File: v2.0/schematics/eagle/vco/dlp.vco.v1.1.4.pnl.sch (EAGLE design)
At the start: 23 parts, among them J1 PWM IN1, J4 EXP.IN1, J6 OSC OUT1

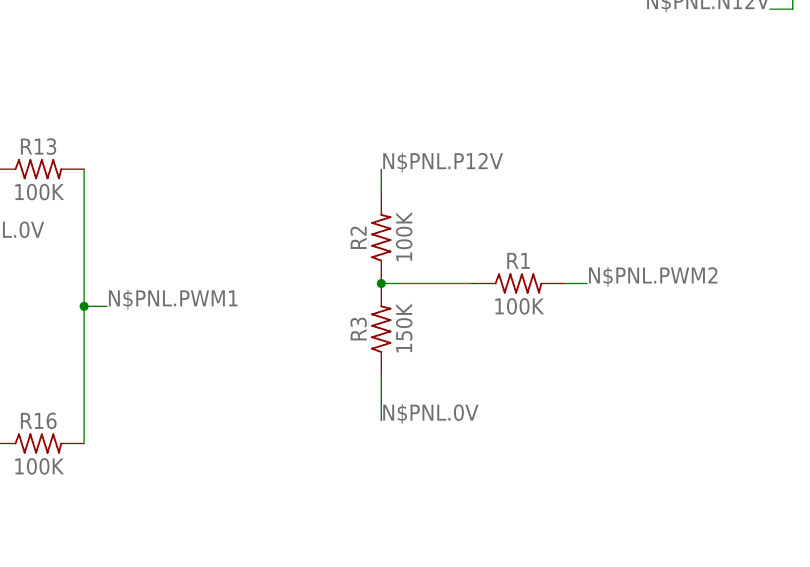
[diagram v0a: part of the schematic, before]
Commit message: Updated values for fixed PWM2
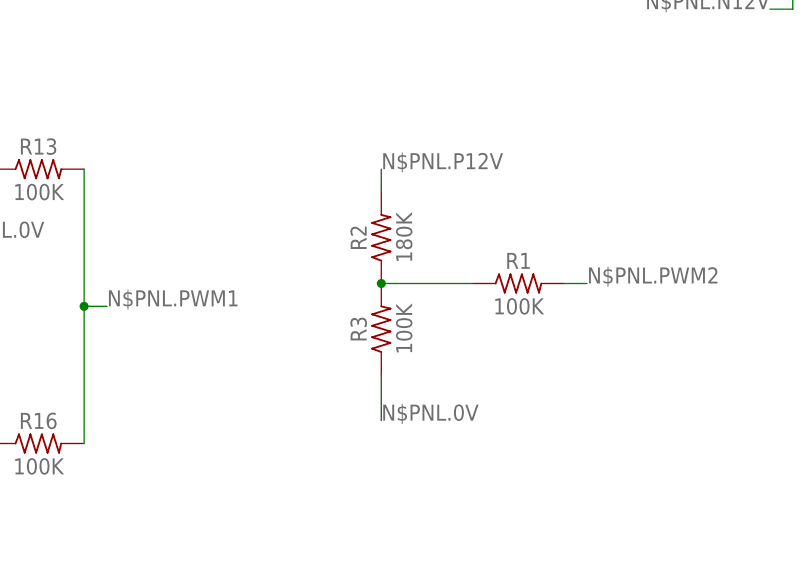
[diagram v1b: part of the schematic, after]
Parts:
- R2: value 100K -> 180K
- R3: value 150K -> 100K
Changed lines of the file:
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@@
 <part name="JP2" library="pinhead" deviceset="PINHD-1X10" device="" value="OSC2"/>
 <part name="R1" library="_common" deviceset="R" device="0309/10" value="100K"/>
-<part name="R2" library="_common" deviceset="R" device="0309/10" value="100K"/>
-<part name="R3" library="_common" deviceset="R" device="0309/10" value="150K"/>
+<part name="R2" library="_common" deviceset="R" device="0309/10" value="180K"/>
+<part name="R3" library="_common" deviceset="R" device="0309/10" value="100K"/>
 <part name="SW-LEVEL2" library="_common" deviceset="R-VAR" device="" value="50K (log)"/>
 <part name="SQ-LEVEL2" library="_common" deviceset="R-VAR" device="" value="50K (log)"/>

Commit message: Split EXP1 and 2 and added EXP2 IN Removed PWM1 ATT and added PWM2
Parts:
- removed R16, R3: 100K, _common:R0309/10
- removed R2: 180K, _common:R0309/10
- added J2: EXP.IN2, _common:JACK-M
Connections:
- removed net N$1: R1.1, R2.1, R3.2
- new net N$6: J2.HOT, R4/2.A
- net N$19: now also R1.1; no longer R16.1
- net N$4: no longer R4/2.A
- net N$PNL.0V: now also J2.GND; no longer R3.1
- net N$PNL.P12V: no longer R2.2
- net N$PNL.PWM1: no longer R16.2
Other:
- moved on the sheet: PWM1, R1
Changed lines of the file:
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@@
 <part name="PWM.ATT1" library="_common" deviceset="R-VAR" device="" value="250K (lin)"/>
 <part name="R13" library="_common" deviceset="R" device="0309/10" value="100K"/>
-<part name="R16" library="_common" deviceset="R" device="0309/10" value="100K"/>
 <part name="JP1" library="pinhead" deviceset="PINHD-1X10" device="" value="OSC1"/>
 <part name="JP2" library="pinhead" deviceset="PINHD-1X10" device="" value="OSC2"/>
 <part name="R1" library="_common" deviceset="R" device="0309/10" value="100K"/>
-<part name="R2" library="_common" deviceset="R" device="0309/10" value="180K"/>
-<part name="R3" library="_common" deviceset="R" device="0309/10" value="100K"/>
 <part name="SW-LEVEL2" library="_common" deviceset="R-VAR" device="" value="50K (log)"/>
 <part name="SQ-LEVEL2" library="_common" deviceset="R-VAR" device="" value="50K (log)"/>
@@
 <part name="R6" library="_common" deviceset="R" device="0309/10" value="100K"/>
 <part name="TUNE2" library="_common" deviceset="R-VAR" device="" value="250K (lin)"/>
+<part name="J2" library="_common" deviceset="JACK-M" device="" value="EXP.IN2"/>
 </parts>
 <sheets>
@@
 <instances>
 <instance part="J1" gate="G$1" x="5.08" y="17.78"/>
-<instance part="PWM1" gate="G$1" x="7.62" y="-20.32" rot="R270"/>
+<instance part="PWM1" gate="G$1" x="48.26" y="-10.16" rot="R270"/>
 <instance part="R14" gate="G$1" x="27.94" y="66.04" rot="R180"/>
 <instance part="R15" gate="G$1" x="17.78" y="35.56"/>
@@
 <instance part="PWM.ATT1" gate="G$1" x="12.7" y="10.16" rot="R270"/>
 <instance part="R13" gate="G$1" x="27.94" y="10.16"/>
-<instance part="R16" gate="G$1" x="27.94" y="-20.32"/>
 <instance part="JP1" gate="A" x="12.7" y="-53.34" rot="R180"/>
 <instance part="JP2" gate="A" x="55.88" y="-53.34" rot="R180"/>
-<instance part="R1" gate="G$1" x="81.28" y="-2.54"/>
-<instance part="R2" gate="G$1" x="66.04" y="2.54" rot="R90"/>
-<instance part="R3" gate="G$1" x="66.04" y="-7.62" rot="R90"/>
+<instance part="R1" gate="G$1" x="68.58" y="-10.16"/>
 <instance part="SW-LEVEL2" gate="G$1" x="147.32" y="10.16" rot="R180"/>
 <instance part="SQ-LEVEL2" gate="G$1" x="147.32" y="-20.32"/>
@@
 <instance part="R6" gate="G$1" x="96.52" y="35.56" rot="MR0"/>
 <instance part="TUNE2" gate="G$1" x="111.76" y="35.56" rot="MR270"/>
+<instance part="J2" gate="G$1" x="73.66" y="71.12" rot="MR0"/>
 </instances>
 <busses>
@@
 <segment>
 <pinref part="PWM1" gate="G$1" pin="P$1"/>
-<pinref part="R16" gate="G$1" pin="1"/>
-<wire x1="12.7" y1="-20.32" x2="22.86" y2="-20.32" width="0.1524" layer="91"/>
+<wire x1="53.34" y1="-10.16" x2="63.5" y2="-10.16" width="0.1524" layer="91"/>
+<pinref part="R1" gate="G$1" pin="1"/>
 </segment>
 </net>
@@
 <segment>
 <pinref part="PWM1" gate="G$1" pin="2"/>
-<wire x1="7.62" y1="-25.4" x2="7.62" y2="-27.94" width="0.1524" layer="91"/>
-<wire x1="7.62" y1="-27.94" x2="12.7" y2="-27.94" width="0.1524" layer="91"/>
-<label x="12.7" y="-27.94" size="1.778" layer="95"/>
+<wire x1="48.26" y1="-15.24" x2="48.26" y2="-17.78" width="0.1524" layer="91"/>
+<wire x1="48.26" y1="-17.78" x2="53.34" y2="-17.78" width="0.1524" layer="91"/>
+<label x="53.34" y="-17.78" size="1.778" layer="95"/>
 </segment>
 <segment>
@@
 </segment>
 <segment>
-<wire x1="66.04" y1="-12.7" x2="66.04" y2="-17.78" width="0.1524" layer="91"/>
-<label x="66.04" y="-17.78" size="1.778" layer="95"/>
-<pinref part="R3" gate="G$1" pin="1"/>
-</segment>
-<segment>
 <label x="76.2" y="53.34" size="1.778" layer="95" rot="MR0"/>
 <wire x1="76.2" y1="58.42" x2="66.04" y2="58.42" width="0.1524" layer="91"/>
@@
 <pinref part="R4" gate="/2" pin="E"/>
 <wire x1="66.04" y1="58.42" x2="66.04" y2="60.96" width="0.1524" layer="91"/>
+<pinref part="J2" gate="G$1" pin="GND"/>
+<wire x1="76.2" y1="68.58" x2="76.2" y2="58.42" width="0.1524" layer="91"/>
+<junction x="76.2" y="58.42"/>
 </segment>
 </net>
@@
 <segment>
 <pinref part="R13" gate="G$1" pin="2"/>
-<pinref part="R16" gate="G$1" pin="2"/>
-<wire x1="33.02" y1="10.16" x2="33.02" y2="-5.08" width="0.1524" layer="91"/>
-<label x="35.56" y="-5.08" size="1.778" layer="95"/>
-<wire x1="33.02" y1="-5.08" x2="33.02" y2="-20.32" width="0.1524" layer="91"/>
-<wire x1="33.02" y1="-5.08" x2="35.56" y2="-5.08" width="0.1524" layer="91"/>
-<junction x="33.02" y="-5.08"/>
+<label x="38.1" y="10.16" size="1.778" layer="95"/>
+<wire x1="33.02" y1="10.16" x2="38.1" y2="10.16" width="0.1524" layer="91"/>
 </segment>
 </net>
@@
 <segment>
 <pinref part="PWM1" gate="G$1" pin="1"/>
-<wire x1="7.62" y1="-15.24" x2="7.62" y2="-12.7" width="0.1524" layer="91"/>
-<wire x1="7.62" y1="-12.7" x2="10.16" y2="-12.7" width="0.1524" layer="91"/>
-<label x="10.16" y="-12.7" size="1.778" layer="95"/>
+<wire x1="48.26" y1="-5.08" x2="48.26" y2="-2.54" width="0.1524" layer="91"/>
+<wire x1="48.26" y1="-2.54" x2="50.8" y2="-2.54" width="0.1524" layer="91"/>
+<label x="50.8" y="-2.54" size="1.778" layer="95"/>
 </segment>
 <segment>
@@
 <wire x1="58.42" y1="-58.42" x2="68.58" y2="-58.42" width="0.1524" layer="91"/>
 <label x="68.58" y="-58.42" size="1.778" layer="95"/>
-</segment>
-<segment>
-<wire x1="66.04" y1="7.62" x2="66.04" y2="10.16" width="0.1524" layer="91"/>
-<label x="66.04" y="10.16" size="1.778" layer="95"/>
-<pinref part="R2" gate="G$1" pin="2"/>
 </segment>
 <segment>
@@
 <segment>
 <pinref part="R1" gate="G$1" pin="2"/>
-<label x="88.9" y="-2.54" size="1.778" layer="95"/>
-<wire x1="86.36" y1="-2.54" x2="88.9" y2="-2.54" width="0.1524" layer="91"/>
+<label x="76.2" y="-10.16" size="1.778" layer="95"/>
+<wire x1="73.66" y1="-10.16" x2="76.2" y2="-10.16" width="0.1524" layer="91"/>
 </segment>
 </net>
@@
 </segment>
 </net>
-<net name="N$1" class="0">
-<segment>
-<pinref part="R1" gate="G$1" pin="1"/>
-<wire x1="66.04" y1="-2.54" x2="76.2" y2="-2.54" width="0.1524" layer="91"/>
-<pinref part="R3" gate="G$1" pin="2"/>
-<pinref part="R2" gate="G$1" pin="1"/>
-<junction x="66.04" y="-2.54"/>
-</segment>
-</net>
 <net name="N$2" class="0">
 <segment>
@@
 <net name="N$4" class="0">
 <segment>
-<pinref part="R4" gate="/2" pin="A"/>
-<wire x1="66.04" y1="73.66" x2="66.04" y2="71.12" width="0.1524" layer="91"/>
 <pinref part="J4" gate="G$1" pin="HOT"/>
 <wire x1="48.26" y1="71.12" x2="48.26" y2="73.66" width="0.1524" layer="91"/>
 <wire x1="48.26" y1="73.66" x2="45.72" y2="73.66" width="0.1524" layer="91"/>
 <pinref part="R4" gate="/1" pin="E"/>
-<wire x1="66.04" y1="73.66" x2="48.26" y2="73.66" width="0.1524" layer="91"/>
-<junction x="48.26" y="73.66"/>
 </segment>
 </net>
@@
 </segment>
 </net>
+<net name="N$6" class="0">
+<segment>
+<pinref part="R4" gate="/2" pin="A"/>
+<wire x1="68.58" y1="73.66" x2="66.04" y2="73.66" width="0.1524" layer="91"/>
+<wire x1="66.04" y1="73.66" x2="66.04" y2="71.12" width="0.1524" layer="91"/>
+<pinref part="J2" gate="G$1" pin="HOT"/>
+</segment>
+</net>

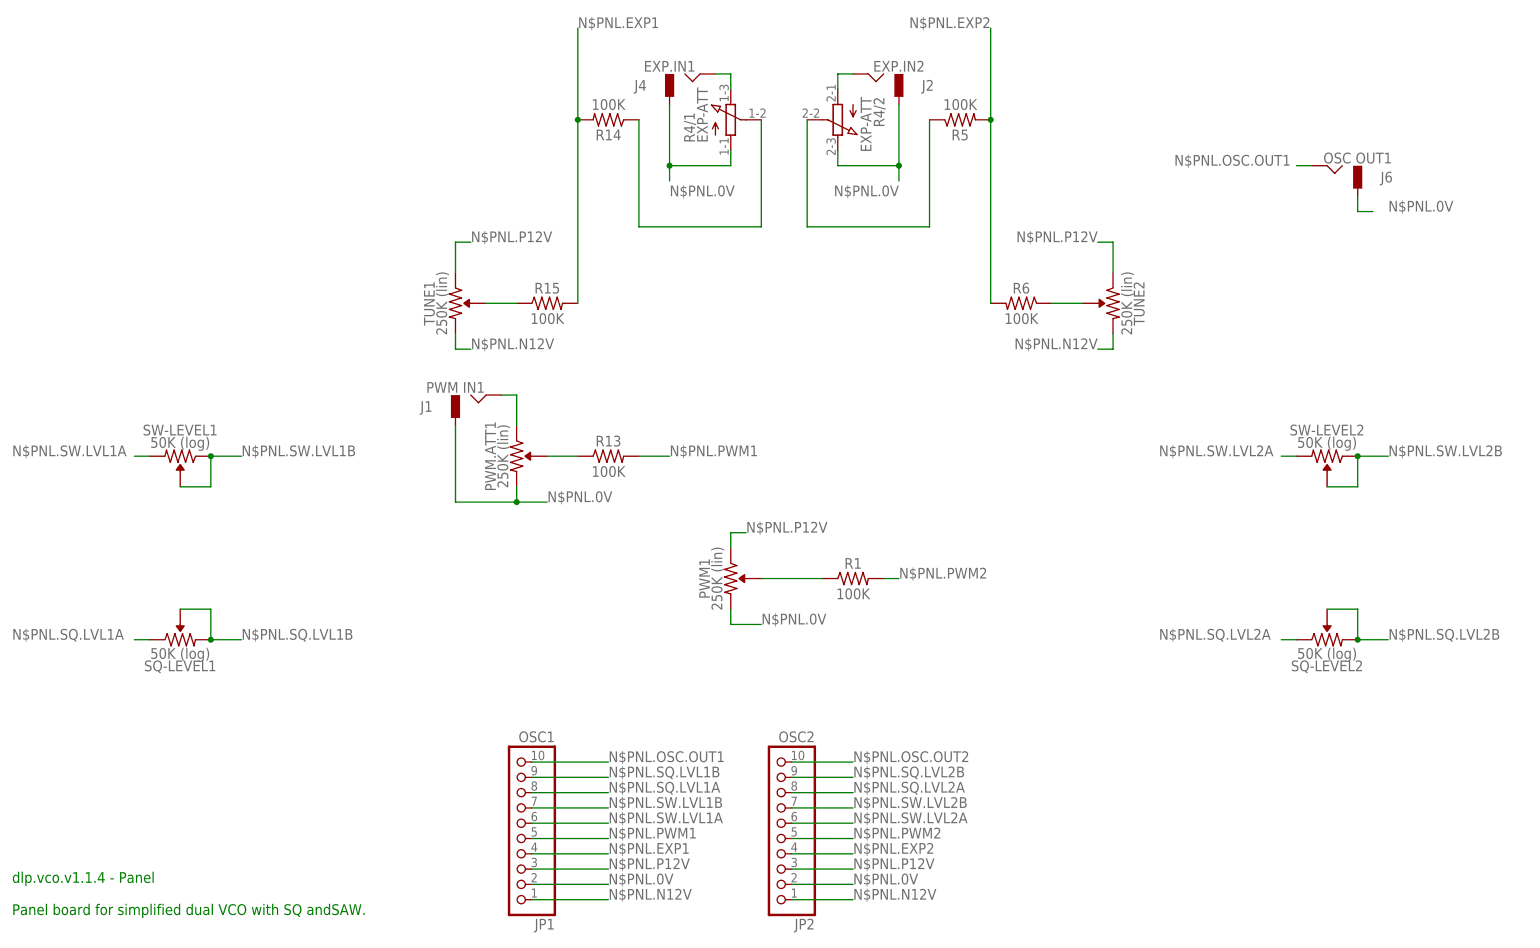
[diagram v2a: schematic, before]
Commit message: Created pannel board and inital layout Updated common libraries for pannel layout and pin tracking
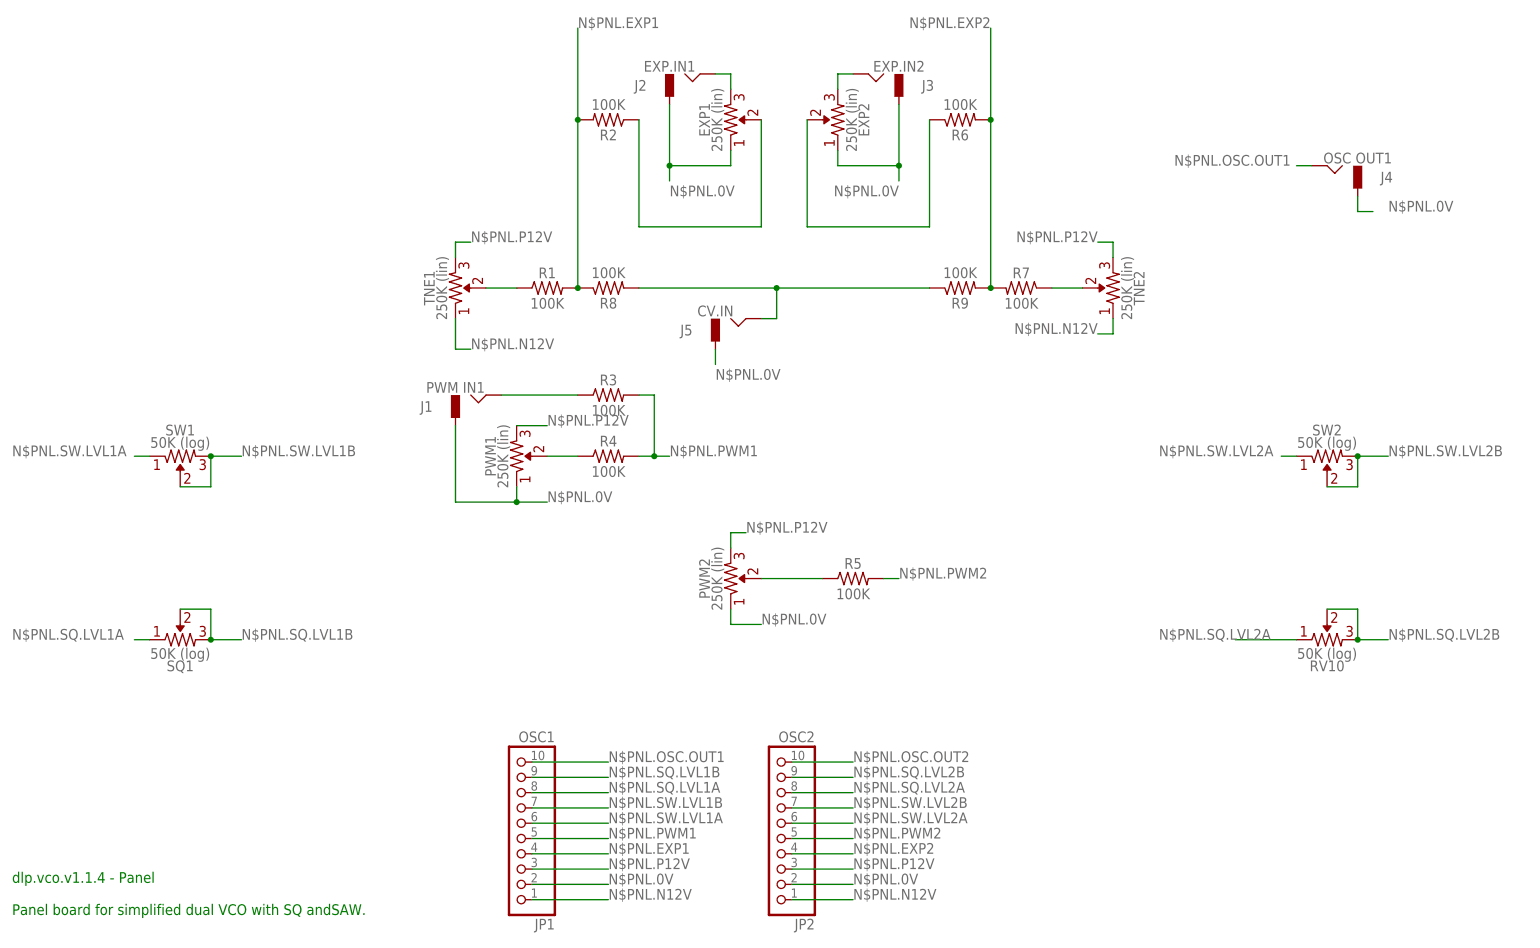
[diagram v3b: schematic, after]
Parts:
- removed J6: OSC OUT1, _common:JACK-M
- removed PWM.ATT1, TUNE1, TUNE2: 250K (lin), _common:R-VAR
- removed R13, R15: 100K, _common:R0309/10
- added EXP1, EXP2, PWM2, TNE1, TNE2: 250K (lin), _common:R-VAR
- added J3: EXP.IN2, _common:JACK-M
- added J5: CV.IN, _common:JACK-M
- added R3, R7, R8, R9: 100K, _common:R0309/10
- J2: value EXP.IN2 -> EXP.IN1
- J4: value EXP.IN1 -> OSC OUT1
- R4: value EXP-ATT -> 100K; device pot:3RP/1610G -> _common:R0309/10
- renumbered R14 to R2, SQ-LEVEL1 to SQ1, SQ-LEVEL2 to RV10, SW-LEVEL1 to SW1, SW-LEVEL2 to SW2
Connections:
- removed net N$25: J1.HOT, PWM.ATT1.1
- new net N$1: J5.HOT, R8.2, R9.1
- new net N$7: J1.HOT, R3.1
- net N$10: now also PWM1.P$1, R4.1; no longer PWM.ATT1.P$1, R13.1
- net N$19: now also PWM2.P$1, R5.1; no longer PWM1.P$1, R1.1
- net N$2: now also EXP1.P$1; no longer R4/1.S
- net N$24: now also R1.1, TNE1.P$1; no longer R15.1, TUNE1.P$1
- net N$3: now also R7.1, TNE2.P$1; no longer R6.1, TUNE2.P$1
- net N$4: now also EXP1.2, J2.HOT; no longer J4.HOT, R4/1.E
- net N$5: now also EXP2.P$1, R6.1; no longer R4/2.S, R5.1
- net N$6: now also EXP2.2, J3.HOT; no longer J2.HOT, R4/2.A
- net N$PNL.0V: now also EXP1.1, EXP2.1, J3.GND, J5.GND, PWM1.1, PWM2.1; no longer J6.GND, PWM.ATT1.2, PWM1.2, R4/1.A, R4/2.E
- net N$PNL.EXP1: now also R1.2, R8.1; no longer R15.2
- net N$PNL.EXP2: now also R7.2, R9.2; no longer R5.2
- net N$PNL.N12V: now also TNE1.1, TNE2.1; no longer TUNE1.2, TUNE2.2
- net N$PNL.OSC.OUT1: now also J4.HOT; no longer J6.HOT
- net N$PNL.P12V: now also PWM1.2, PWM2.2, TNE1.2, TNE2.2; no longer PWM1.1, TUNE1.1, TUNE2.1
- net N$PNL.PWM1: now also R3.2, R4.2; no longer R13.2
- net N$PNL.PWM2: now also R5.2; no longer R1.2
- net N$PNL.SW.LVL1A: now also SW1.1; no longer SW1.2
- net N$PNL.SW.LVL1B: now also SW1.2; no longer SW1.1
- net N$PNL.SW.LVL2A: now also SW2.1; no longer SW2.2
- net N$PNL.SW.LVL2B: now also SW2.2; no longer SW2.1
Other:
- moved on the sheet: J2, J4, R1, R5, R6

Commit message: Reduced size of vco pannel and applied routing
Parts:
- renumbered RV10 to SQ2
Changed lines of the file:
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@@
 <part name="R5" library="_common" deviceset="R" device="0309/10" value="100K"/>
 <part name="SW2" library="_common" deviceset="R-VAR" device="" value="50K (log)"/>
-<part name="RV10" library="_common" deviceset="R-VAR" device="" value="50K (log)"/>
+<part name="SQ2" library="_common" deviceset="R-VAR" device="" value="50K (log)"/>
 <part name="R6" library="_common" deviceset="R" device="0309/10" value="100K"/>
 <part name="R7" library="_common" deviceset="R" device="0309/10" value="100K"/>
@@
 <instance part="R5" gate="G$1" x="68.58" y="-10.16"/>
 <instance part="SW2" gate="G$1" x="147.32" y="10.16" rot="MR180"/>
-<instance part="RV10" gate="G$1" x="147.32" y="-20.32"/>
+<instance part="SQ2" gate="G$1" x="147.32" y="-20.32"/>
 <instance part="R6" gate="G$1" x="86.36" y="66.04" rot="MR180"/>
 <instance part="R7" gate="G$1" x="96.52" y="38.1" rot="MR0"/>
@@
 </segment>
 <segment>
-<pinref part="RV10" gate="G$1" pin="1"/>
+<pinref part="SQ2" gate="G$1" pin="1"/>
 <wire x1="142.24" y1="-20.32" x2="132.08" y2="-20.32" width="0.1524" layer="91"/>
 <label x="119.38" y="-20.32" size="1.778" layer="95"/>
@@
 </segment>
 <segment>
-<pinref part="RV10" gate="G$1" pin="2"/>
+<pinref part="SQ2" gate="G$1" pin="2"/>
 <wire x1="152.4" y1="-20.32" x2="152.4" y2="-15.24" width="0.1524" layer="91"/>
-<pinref part="RV10" gate="G$1" pin="P$1"/>
+<pinref part="SQ2" gate="G$1" pin="P$1"/>
 <wire x1="147.32" y1="-15.24" x2="152.4" y2="-15.24" width="0.1524" layer="91"/>
 <wire x1="152.4" y1="-20.32" x2="157.48" y2="-20.32" width="0.1524" layer="91"/>
